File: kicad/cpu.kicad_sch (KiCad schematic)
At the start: 13 parts, among them SW1 RESET, U1 W65C816S, U2 74HC573, U3 ATF22V10C 816DEC02, X1 12MHz

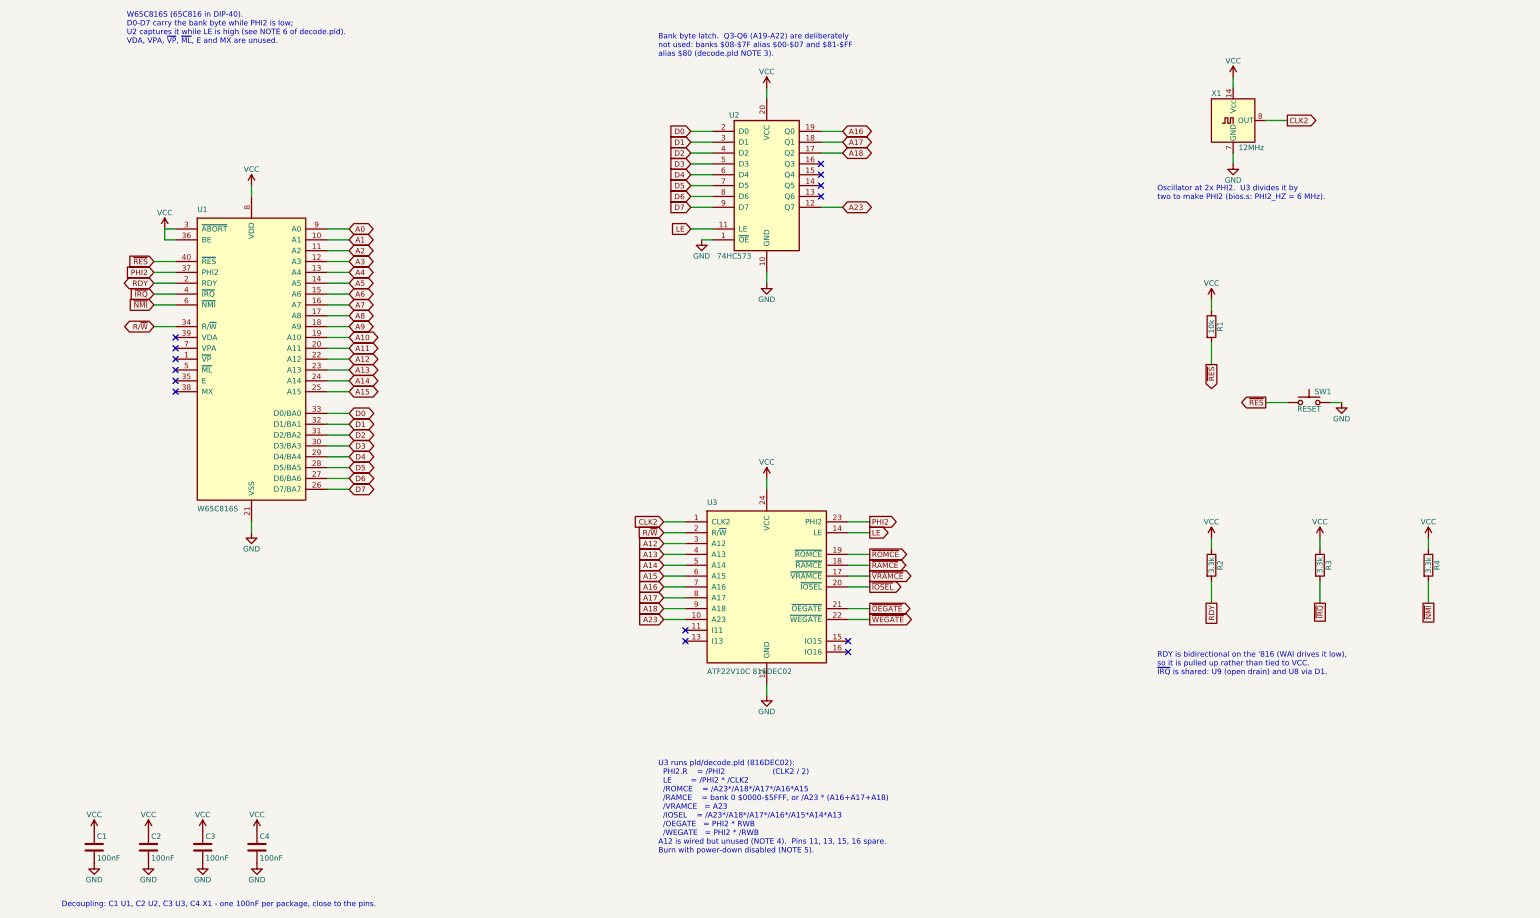
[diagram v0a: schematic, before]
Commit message: Update KiCad schematic to match the build as wired
- Remove video RAM (future expansion); GAL ~{VRAMCE} is NC and
  ~{WEGATE} goes only to the RAM
- VIA is a W65C22N6TPG-14: IRQB wired directly to ~{IRQ} (no diode)
- RDY and ~{NMI} tied directly to +5V; only reset and ~{IRQ} pull-ups
- ACIA clocked by a 1.8432 MHz DIP-8 oscillator on XTLI (EN high)
- Serial through a MAX232N to a female DB9 (pins 2, 3, 8, 5)
- VIA Port B drives eight LEDs with series resistors; Port A, CA/CB NC
- Drop per-chip decoupling; single 0.1uF electrolytic at the supply
- Unknown resistor values shown as '?'
- Update kicad/README.md and README.md accordingly

Co-Authored-By: Claude Opus 5.5 <noreply@anthropic.com>
Claude-Session: https://claude.ai/code/session_01GgTWzZQQJPzWrEMiSDZH6j
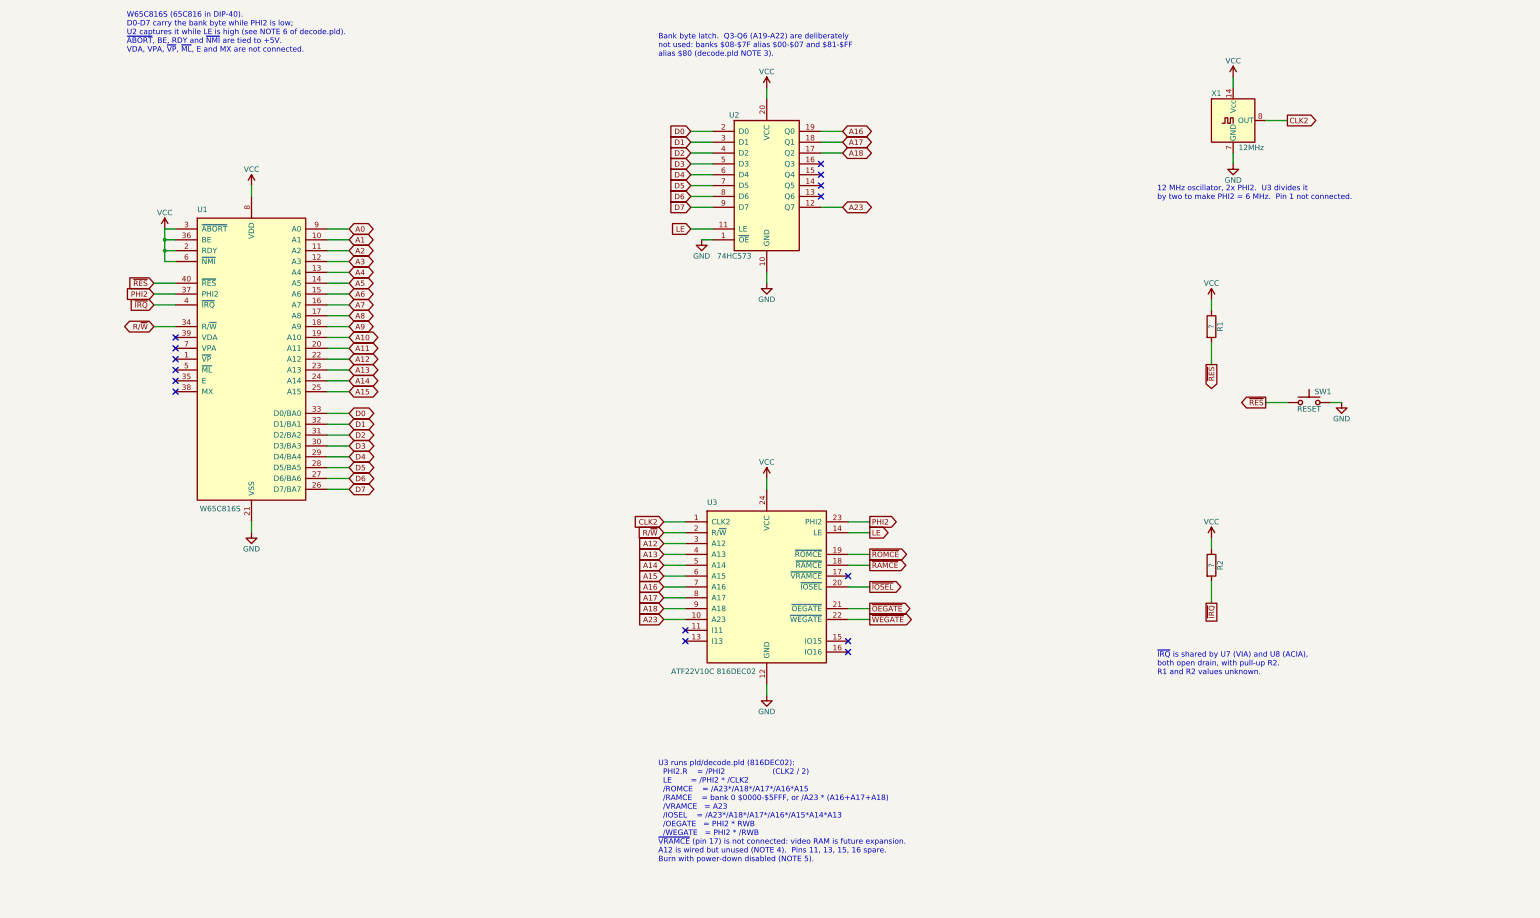
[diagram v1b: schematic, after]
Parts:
- removed C1, C2, C3, C4: 100nF, symbol be6502:C
- removed R3, R4: 3.3k, symbol be6502:R
- R1: value 10k -> ?
- R2: value 3.3k -> ?
- U2: footprint (none) -> Package_DIP:DIP-20_W7.62mm
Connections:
- net ~{NMI} is gone; now on net VCC: U1.6 (~{NMI})
- net VCC: now also U1.2 (RDY)
- net ~{IRQ}: now also R2.2
- removed net RDY: R2.2, U1.2 (RDY)
- net ~{VRAMCE}: no longer names the net of U3.17 (~{VRAMCE})
- no-connect marks 14 -> 15
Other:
- note added: "12 MHz oscillator, 2x PHI2. U3 divides it by two to make PHI2 = 6 MHz. Pin 1 not connected."
- note added: "U3 runs pld/decode.pld (816DEC02): PHI2.R = /PHI2 (CLK2 / 2) LE = /PHI2 * /CLK2 /ROMCE = /A23*/A18*/A17*/A16*A15 /RAMCE = bank 0 $0000-$5FFF, or /A23 * (A16+A17+A18) /VRAMCE = A23 /IOSEL = /A23*/A18*/A17*/A16*/A15*A14*A13 /OEGATE = PHI2 * RWB /WEGATE = PHI2 * /RWB ~{VRAMCE} (pin 17) is not connected: video RAM is future expansion. A12 is wired but unused (NOTE 4). Pins 11, 13, 15, 16 spare. Burn 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"
- note added: "W65C816S (65C816 in DIP-40). D0-D7 carry the bank byte while PHI2 is low; U2 captures it while LE is high (see NOTE 6 of decode.pld). ~{ABORT}, BE, RDY and ~{NMI} are tied to +5V. VDA, VPA, ~{VP}, ~{ML}, E and MX are not connected."
- note added: "~{IRQ} is shared by U7 (VIA) and U8 (ACIA), both open drain, with pull-up R2. R1 and R2 values unknown."
- note removed: "Decoupling: C1 U1, C2 U2, C3 U3, C4 X1 - one 100nF per package, close to the pins."
- note removed: "Oscillator at 2x PHI2. U3 divides it by two to make PHI2 (bios.s: PHI2_HZ = 6 MHz)."
- note removed: "RDY is bidirectional on the '816 (WAI drives it low), so it is pulled up rather than tied to VCC. ~{IRQ} is shared: U9 (open drain) and U8 via D1."
- note removed: "U3 runs pld/decode.pld (816DEC02): PHI2.R = /PHI2 (CLK2 / 2) LE = /PHI2 * /CLK2 /ROMCE = /A23*/A18*/A17*/A16*A15 /RAMCE = bank 0 $0000-$5FFF, or /A23 * (A16+A17+A18) /VRAMCE = A23 /IOSEL = /A23*/A18*/A17*/A16*/A15*A14*A13 /OEGATE = PHI2 * RWB /WEGATE = PHI2 * /RWB A12 is wired but unused (NOTE 4). Pins 11, 13, 15, 16 spare. Burn with power-down disabled (NOTE 5)."
- note removed: "W65C816S (65C816 in DIP-40). D0-D7 carry the bank byte while PHI2 is low; U2 captures it while LE is high (see NOTE 6 of decode.pld). VDA, VPA, ~{VP}, ~{ML}, E and MX are unused."

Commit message: Show resistors R1-R10 as 1k (estimated)
The markings are unreadable; 1k is the builder's estimate and is noted
as such on the sheets and in kicad/README.md. Also list the unconnected
DB9 pins explicitly.

Co-Authored-By: Claude Opus 5.5 <noreply@anthropic.com>
Claude-Session: https://claude.ai/code/session_01GgTWzZQQJPzWrEMiSDZH6j
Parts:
- R1, R2: value ? -> 1k
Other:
- note added: "~{IRQ} is shared by U7 (VIA) and U8 (ACIA), both open drain, with pull-up R2. R1, R2: 1k (estimated; markings unreadable)."
- note removed: "~{IRQ} is shared by U7 (VIA) and U8 (ACIA), both open drain, with pull-up R2. R1 and R2 values unknown."
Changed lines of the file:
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@@
 (symbol (lib_id "be6502:GND") (at 309.88 60.96 0) (unit 1) (in_bom no) (on_board no) (dnp no) (property "Reference" "#PWR010" (at 309.88 67.31 0) (effects (font (size 1.27 1.27)) hide)) (property "Value" "GND" (at 309.88 64.77 0) (effects (font (size 1.27 1.27)))) (property "Footprint" "" (at 309.88 60.96 0) (effects (font (size 1.27 1.27)) hide)) (property "Datasheet" "" (at 309.88 60.96 0) (effects (font (size 1.27 1.27)) hide)) (pin "1") (instances (project "be6502" (path "/c8451a90-6bbf-595d-a4c9-ea2cdd0996a1/f67db34f-3d17-54e5-a1b6-ae57793ddc10" (reference "#PWR010") (unit 1)))))
 (text "12 MHz oscillator, 2x PHI2.  U3 divides it\nby two to make PHI2 = 6 MHz.  Pin 1 not connected." (at 292.1 66.04 0) (effects (font (size 1.27 1.27)) (justify left top)))
-(symbol (lib_id "be6502:R") (at 304.8 99.06 0) (unit 1) (in_bom yes) (on_board yes) (dnp no) (property "Reference" "R1" (at 306.832 99.06 90) (effects (font (size 1.27 1.27)))) (property "Value" "?" (at 304.8 99.06 90) (effects (font (size 1.27 1.27)))) (property "Footprint" "" (at 303.022 99.06 90) (effects (font (size 1.27 1.27)) hide)) (property "Datasheet" "~" (at 304.8 99.06 0) (effects (font (size 1.27 1.27)) hide)) (pin "1") (pin "2") (instances (project "be6502" (path "/c8451a90-6bbf-595d-a4c9-ea2cdd0996a1/f67db34f-3d17-54e5-a1b6-ae57793ddc10" (reference "R1") (unit 1)))))
+(symbol (lib_id "be6502:R") (at 304.8 99.06 0) (unit 1) (in_bom yes) (on_board yes) (dnp no) (property "Reference" "R1" (at 306.832 99.06 90) (effects (font (size 1.27 1.27)))) (property "Value" "1k" (at 304.8 99.06 90) (effects (font (size 1.27 1.27)))) (property "Footprint" "" (at 303.022 99.06 90) (effects (font (size 1.27 1.27)) hide)) (property "Datasheet" "~" (at 304.8 99.06 0) (effects (font (size 1.27 1.27)) hide)) (pin "1") (pin "2") (instances (project "be6502" (path "/c8451a90-6bbf-595d-a4c9-ea2cdd0996a1/f67db34f-3d17-54e5-a1b6-ae57793ddc10" (reference "R1") (unit 1)))))
 (wire (pts (xy 304.8 95.25) (xy 304.8 92.71)) (stroke (width 0) (type default)))
 (symbol (lib_id "be6502:VCC") (at 304.8 92.71 0) (unit 1) (in_bom no) (on_board no) (dnp no) (property "Reference" "#PWR011" (at 304.8 96.52 0) (effects (font (size 1.27 1.27)) hide)) (property "Value" "VCC" (at 304.8 88.9 0) (effects (font (size 1.27 1.27)))) (property "Footprint" "" (at 304.8 92.71 0) (effects (font (size 1.27 1.27)) hide)) (property "Datasheet" "" (at 304.8 92.71 0) (effects (font (size 1.27 1.27)) hide)) (pin "1") (instances (project "be6502" (path "/c8451a90-6bbf-595d-a4c9-ea2cdd0996a1/f67db34f-3d17-54e5-a1b6-ae57793ddc10" (reference "#PWR011") (unit 1)))))
@@
 (wire (pts (xy 332.74 116.84) (xy 335.28 116.84)) (stroke (width 0) (type default)))
 (symbol (lib_id "be6502:GND") (at 335.28 116.84 0) (unit 1) (in_bom no) (on_board no) (dnp no) (property "Reference" "#PWR012" (at 335.28 123.19 0) (effects (font (size 1.27 1.27)) hide)) (property "Value" "GND" (at 335.28 120.65 0) (effects (font (size 1.27 1.27)))) (property "Footprint" "" (at 335.28 116.84 0) (effects (font (size 1.27 1.27)) hide)) (property "Datasheet" "" (at 335.28 116.84 0) (effects (font (size 1.27 1.27)) hide)) (pin "1") (instances (project "be6502" (path "/c8451a90-6bbf-595d-a4c9-ea2cdd0996a1/f67db34f-3d17-54e5-a1b6-ae57793ddc10" (reference "#PWR012") (unit 1)))))
-(symbol (lib_id "be6502:R") (at 304.8 154.94 0) (unit 1) (in_bom yes) (on_board yes) (dnp no) (property "Reference" "R2" (at 306.832 154.94 90) (effects (font (size 1.27 1.27)))) (property "Value" "?" (at 304.8 154.94 90) (effects (font (size 1.27 1.27)))) (property "Footprint" "" (at 303.022 154.94 90) (effects (font (size 1.27 1.27)) hide)) (property "Datasheet" "~" (at 304.8 154.94 0) (effects (font (size 1.27 1.27)) hide)) (pin "1") (pin "2") (instances (project "be6502" (path "/c8451a90-6bbf-595d-a4c9-ea2cdd0996a1/f67db34f-3d17-54e5-a1b6-ae57793ddc10" (reference "R2") (unit 1)))))
+(symbol (lib_id "be6502:R") (at 304.8 154.94 0) (unit 1) (in_bom yes) (on_board yes) (dnp no) (property "Reference" "R2" (at 306.832 154.94 90) (effects (font (size 1.27 1.27)))) (property "Value" "1k" (at 304.8 154.94 90) (effects (font (size 1.27 1.27)))) (property "Footprint" "" (at 303.022 154.94 90) (effects (font (size 1.27 1.27)) hide)) (property "Datasheet" "~" (at 304.8 154.94 0) (effects (font (size 1.27 1.27)) hide)) (pin "1") (pin "2") (instances (project "be6502" (path "/c8451a90-6bbf-595d-a4c9-ea2cdd0996a1/f67db34f-3d17-54e5-a1b6-ae57793ddc10" (reference "R2") (unit 1)))))
 (wire (pts (xy 304.8 151.13) (xy 304.8 148.59)) (stroke (width 0) (type default)))
 (symbol (lib_id "be6502:VCC") (at 304.8 148.59 0) (unit 1) (in_bom no) (on_board no) (dnp no) (property "Reference" "#PWR013" (at 304.8 152.4 0) (effects (font (size 1.27 1.27)) hide)) (property "Value" "VCC" (at 304.8 144.78 0) (effects (font (size 1.27 1.27)))) (property "Footprint" "" (at 304.8 148.59 0) (effects (font (size 1.27 1.27)) hide)) (property "Datasheet" "" (at 304.8 148.59 0) (effects (font (size 1.27 1.27)) hide)) (pin "1") (instances (project "be6502" (path "/c8451a90-6bbf-595d-a4c9-ea2cdd0996a1/f67db34f-3d17-54e5-a1b6-ae57793ddc10" (reference "#PWR013") (unit 1)))))
 (wire (pts (xy 304.8 158.75) (xy 304.8 163.83)) (stroke (width 0) (type default)))
 (global_label "~{IRQ}" (shape passive) (at 304.8 163.83 270) (fields_autoplaced) (effects (font (size 1.27 1.27)) (justify right)) (property "Intersheetrefs" "${INTERSHEET_REFS}" (at 304.8 163.83 0) (effects (font (size 1.27 1.27)) (justify right) hide)))
-(text "~{IRQ} is shared by U7 (VIA) and U8 (ACIA),\nboth open drain, with pull-up R2.\nR1 and R2 values unknown." (at 292.1 175.26 0) (effects (font (size 1.27 1.27)) (justify left top)))
+(text "~{IRQ} is shared by U7 (VIA) and U8 (ACIA),\nboth open drain, with pull-up R2.\nR1, R2: 1k (estimated; markings unreadable)." (at 292.1 175.26 0) (effects (font (size 1.27 1.27)) (justify left top)))
 )

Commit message: Mark R1-R10 as measured 1k
Co-Authored-By: Claude Opus 5.5 <noreply@anthropic.com>
Claude-Session: https://claude.ai/code/session_01GgTWzZQQJPzWrEMiSDZH6j
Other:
- note added: "~{IRQ} is shared by U7 (VIA) and U8 (ACIA), both open drain, with pull-up R2. R1, R2: 1k (measured)."
- note removed: "~{IRQ} is shared by U7 (VIA) and U8 (ACIA), both open drain, with pull-up R2. R1, R2: 1k (estimated; markings unreadable)."
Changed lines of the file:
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@@
 (wire (pts (xy 304.8 158.75) (xy 304.8 163.83)) (stroke (width 0) (type default)))
 (global_label "~{IRQ}" (shape passive) (at 304.8 163.83 270) (fields_autoplaced) (effects (font (size 1.27 1.27)) (justify right)) (property "Intersheetrefs" "${INTERSHEET_REFS}" (at 304.8 163.83 0) (effects (font (size 1.27 1.27)) (justify right) hide)))
-(text "~{IRQ} is shared by U7 (VIA) and U8 (ACIA),\nboth open drain, with pull-up R2.\nR1, R2: 1k (estimated; markings unreadable)." (at 292.1 175.26 0) (effects (font (size 1.27 1.27)) (justify left top)))
+(text "~{IRQ} is shared by U7 (VIA) and U8 (ACIA),\nboth open drain, with pull-up R2.\nR1, R2: 1k (measured)." (at 292.1 175.26 0) (effects (font (size 1.27 1.27)) (justify left top)))
 )
